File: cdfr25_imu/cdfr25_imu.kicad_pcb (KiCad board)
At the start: 2 copper layers, 29 x 21 mm, 14 parts, among them J1 Conn_01x06_Pin, U1 LSM6DSL, U2 LIS2MDL

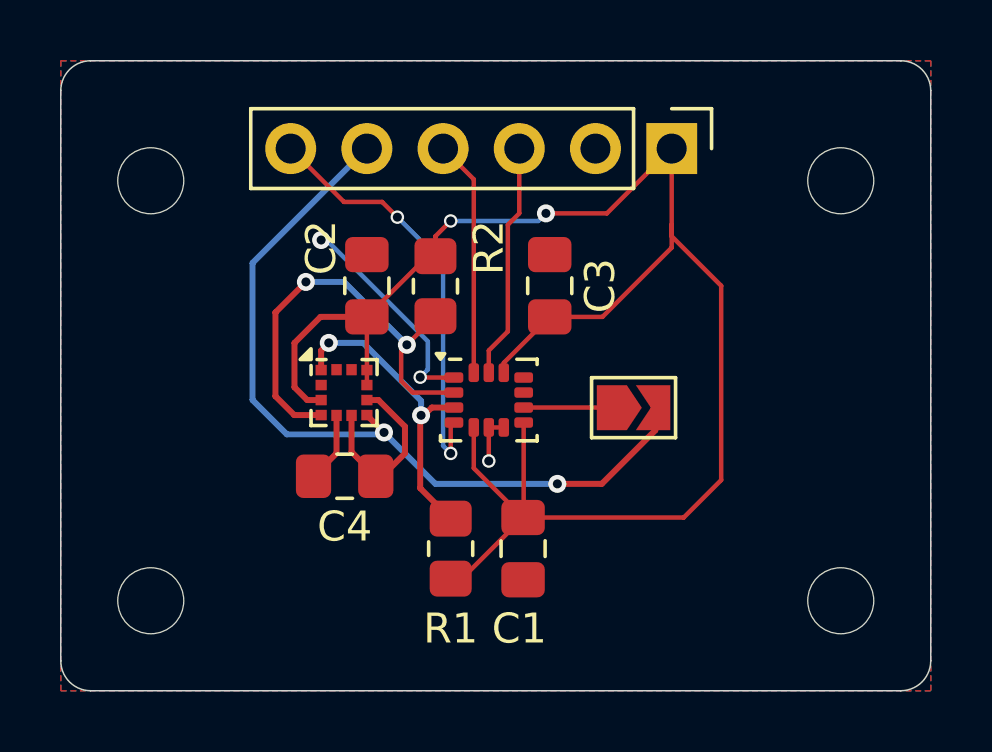
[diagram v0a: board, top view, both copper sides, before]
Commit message: Fix clearance problem
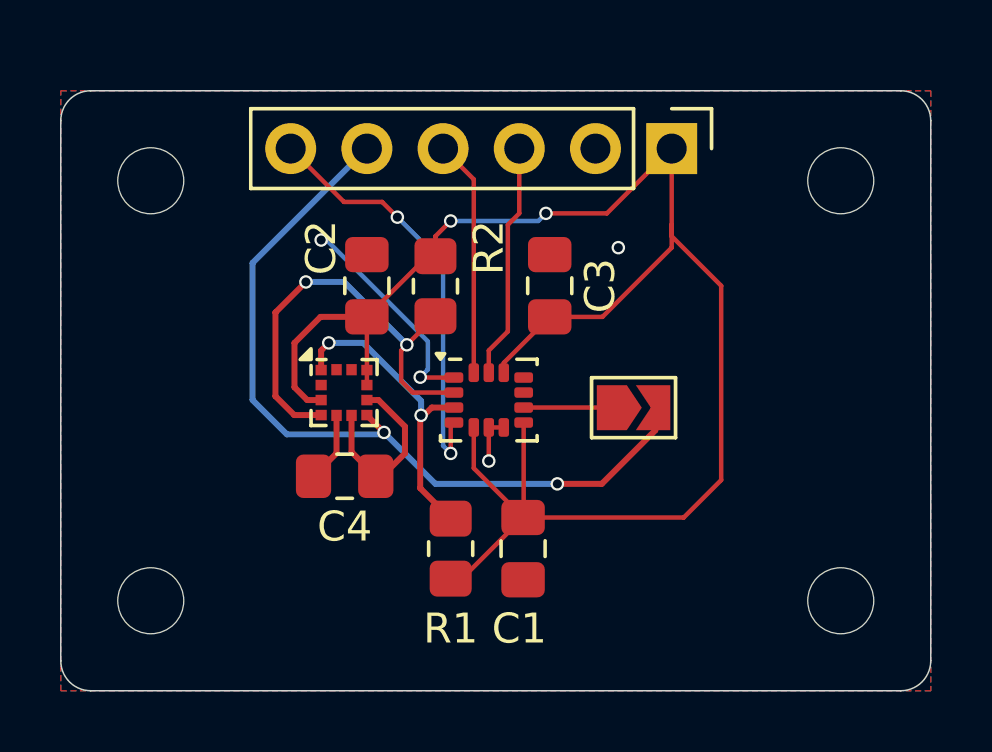
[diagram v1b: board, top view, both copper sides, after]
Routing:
- net GND: vias 3 -> 4
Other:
- board size 29 x 21 mm -> 29 x 20 mm
- board text added: "GND"
- board text added: "INT1"
- board text added: "INT2"
- board text added: "SCL"
- board text added: "SDA"
- board text added: "VCC"
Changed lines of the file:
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@@
 		)
 		(property ki_fp_filters "C_*")
-		(sheetname "Racine")
+		(sheetname "Root")
 		(sheetfile "cdfr25_imu.kicad_sch")
 		(attr smd)
@@
 		)
 		(property ki_fp_filters "R_*")
-		(sheetname "Racine")
+		(sheetname "Root")
 		(sheetfile "cdfr25_imu.kicad_sch")
 		(attr smd)
@@
 		)
 		(property ki_fp_filters "MountingHole*")
-		(sheetname "Racine")
+		(sheetname "Root")
 		(sheetfile "cdfr25_imu.kicad_sch")
 		(attr exclude_from_pos_files)
@@
 		)
 		(property ki_fp_filters "R_*")
-		(sheetname "Racine")
+		(sheetname "Root")
 		(sheetfile "cdfr25_imu.kicad_sch")
 		(attr smd)
@@
 		)
 		(property ki_fp_filters "C_*")
-		(sheetname "Racine")
+		(sheetname "Root")
 		(sheetfile "cdfr25_imu.kicad_sch")
 		(attr smd)
@@
 		)
 		(property ki_fp_filters "MountingHole*")
-		(sheetname "Racine")
+		(sheetname "Root")
 		(sheetfile "cdfr25_imu.kicad_sch")
 		(attr exclude_from_pos_files)
@@
 		)
 		(property ki_fp_filters "MountingHole*")
-		(sheetname "Racine")
+		(sheetname "Root")
 		(sheetfile "cdfr25_imu.kicad_sch")
 		(attr exclude_from_pos_files)
@@
 		)
 		(property ki_fp_filters "Connector*:*_1x??_*")
-		(sheetname "Racine")
+		(sheetname "Root")
 		(sheetfile "cdfr25_imu.kicad_sch")
 		(attr through_hole)
@@
 		)
 		(property ki_fp_filters "LGA*2x2mm*P0.5mm*")
-		(sheetname "Racine")
+		(sheetname "Root")
 		(sheetfile "cdfr25_imu.kicad_sch")
 		(attr smd)
@@
 		)
 		(property ki_fp_filters "SolderJumper*Open*")
-		(sheetname "Racine")
+		(sheetname "Root")
 		(sheetfile "cdfr25_imu.kicad_sch")
 		(zone_connect 1)
@@
 		)
 		(property ki_fp_filters "MountingHole*")
-		(sheetname "Racine")
+		(sheetname "Root")
 		(sheetfile "cdfr25_imu.kicad_sch")
 		(attr exclude_from_pos_files)
@@
 		)
 		(property ki_fp_filters "LGA*3x2.5mm*P0.5mm*LayoutBorder3x4y*")
-		(sheetname "Racine")
+		(sheetname "Root")
 		(sheetfile "cdfr25_imu.kicad_sch")
 		(attr smd)
@@
 		)
 		(property ki_fp_filters "C_*")
-		(sheetname "Racine")
+		(sheetname "Root")
 		(sheetfile "cdfr25_imu.kicad_sch")
 		(attr smd)
@@
 		)
 		(property ki_fp_filters "C_*")
-		(sheetname "Racine")
+		(sheetname "Root")
 		(sheetfile "cdfr25_imu.kicad_sch")
 		(attr smd)
@@
 	)
 	(gr_line
-		(start 99 56)
-		(end 126 56)
+		(start 99 57)
+		(end 126 57)
 		(stroke
 			(width 0.05)
@@
 		(layer "Edge.Cuts")
 	)
-	(gr_arc
-		(start 98 57)
-		(mid 98.292893 56.292893)
-		(end 99 56)
+	(gr_line
+		(start 126 77)
+		(end 99 77)
 		(stroke
 			(width 0.05)
@@
 	)
 	(gr_line
-		(start 127 57)
+		(start 127 58)
 		(end 127 76)
 		(stroke
@@
 	)
 	(gr_arc
-		(start 126 56)
-		(mid 126.707107 56.292893)
-		(end 127 57)
+		(start 126 57)
+		(mid 126.707107 57.292893)
+		(end 127 58)
 		(stroke
 			(width 0.05)
@@
 		(layer "Edge.Cuts")
 	)
-	(gr_line
-		(start 98 76)
-		(end 98 57)
+	(gr_arc
+		(start 98 58)
+		(mid 98.292893 57.292893)
+		(end 99 57)
 		(stroke
 			(width 0.05)
@@
 	)
 	(gr_line
-		(start 126 77)
-		(end 99 77)
+		(start 98 76)
+		(end 98 58)
 		(stroke
 			(width 0.05)
@@
 		(layer "Edge.Cuts")
 	)
+	(gr_text "GND"
+		(at 115.316 63.754 -90)
+		(layer "B.SilkS")
+		(effects
+			(font
+				(size 1 1)
+				(thickness 0.1)
+			)
+			(justify left bottom mirror)
+		)
+	)
+	(gr_text "INT2"
+		(at 105.156 64.008 -90)
+		(layer "B.SilkS")
+		(effects
+			(font
+				(size 1 1)
+				(thickness 0.1)
+			)
+			(justify left bottom mirror)
+		)
+	)
+	(gr_text "INT1"
+		(at 107.696 64.008 -90)
+		(layer "B.SilkS")
+		(effects
+			(font
+				(size 1 1)
+				(thickness 0.1)
+			)
+			(justify left bottom mirror)
+		)
+	)
+	(gr_text "SDA"
+		(at 110.236 63.754 -90)
+		(layer "B.SilkS")
+		(effects
+			(font
+				(size 1 1)
+				(thickness 0.1)
+			)
+			(justify left bottom mirror)
+		)
+	)
+	(gr_text "VCC"
+		(at 117.856 63.754 -90)
+		(layer "B.SilkS")
+		(effects
+			(font
+				(size 1 1)
+				(thickness 0.1)
+			)
+			(justify left bottom mirror)
+		)
+	)
+	(gr_text "SCL"
+		(at 112.776 63.754 -90)
+		(layer "B.SilkS")
+		(effects
+			(font
+				(size 1 1)
+				(thickness 0.1)
+			)
+			(justify left bottom mirror)
+		)
+	)
 	(segment
 		(start 112.268 68.2225)
@@
 	(via
 		(at 106.68 61.976)
-		(size 0.6)
+		(size 0.45)
 		(drill 0.3)
 		(layers "F.Cu" "B.Cu")
@@
 		(net 1)
 	)
+	(via
+		(at 116.586 62.23)
+		(size 0.45)
+		(drill 0.3)
+		(layers "F.Cu" "B.Cu")
+		(free yes)
+		(net 1)
+	)
 	(segment
 		(start 109.982 66.548)
@@
 	(via
 		(at 114.173 61.087)
-		(size 0.6)
+		(size 0.45)
 		(drill 0.3)
 		(layers "F.Cu" "B.Cu")
@@
 	(via
 		(at 114.554 70.104)
-		(size 0.6)
+		(size 0.45)
 		(drill 0.3)
 		(layers "F.Cu" "B.Cu")
@@
 	(via
 		(at 108.7755 68.3895)
-		(size 0.6)
+		(size 0.45)
 		(drill 0.3)
 		(layers "F.Cu" "B.Cu")
@@
 	(via
 		(at 109.5375 65.4685)
-		(size 0.6)
+		(size 0.45)
 		(drill 0.3)
 		(layers "F.Cu" "B.Cu")
@@
 	(via
 		(at 106.172 63.373)
-		(size 0.6)
+		(size 0.45)
 		(drill 0.3)
 		(layers "F.Cu" "B.Cu")
@@
 	(via
 		(at 110.010908 67.819234)
-		(size 0.6)
+		(size 0.45)
 		(drill 0.3)
 		(layers "F.Cu" "B.Cu")
@@
 	(via
 		(at 106.934 65.405)
-		(size 0.6)
+		(size 0.45)
 		(drill 0.3)
 		(layers "F.Cu" "B.Cu")
@@
 		(polygon
 			(pts
-				(xy 98 56) (xy 127 56) (xy 127 77) (xy 98 77)
+				(xy 98 57) (xy 127 57) (xy 127 77) (xy 98 77)
 			)
 		)

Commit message: Add marking
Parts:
- H1, H2, H3, H4: value MountingHole -> MountingHole_Pad; footprint MountingHole:MountingHole_2.2mm_M2 -> MountingHole:MountingHole_2.2mm_M2_Pad_Via
- moved H2 26.9 mm to (101.0, 74.0)
- moved H3 26.9 mm to (124.0, 60.0)
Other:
- board text added: "X"
- board text added: "Y"
- board text added: "Z"
